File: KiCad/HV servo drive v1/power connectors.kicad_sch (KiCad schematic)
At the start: 12 parts, among them J10 DC BUS J2, J5 MOTOR, J7 DC BUS J1

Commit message: KiCad 8.0 update
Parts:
- renumbered C8 to C48, C9 to C49, C48 to C8, C49 to C9, J5 to J2, J7 to J4, J10 to J5

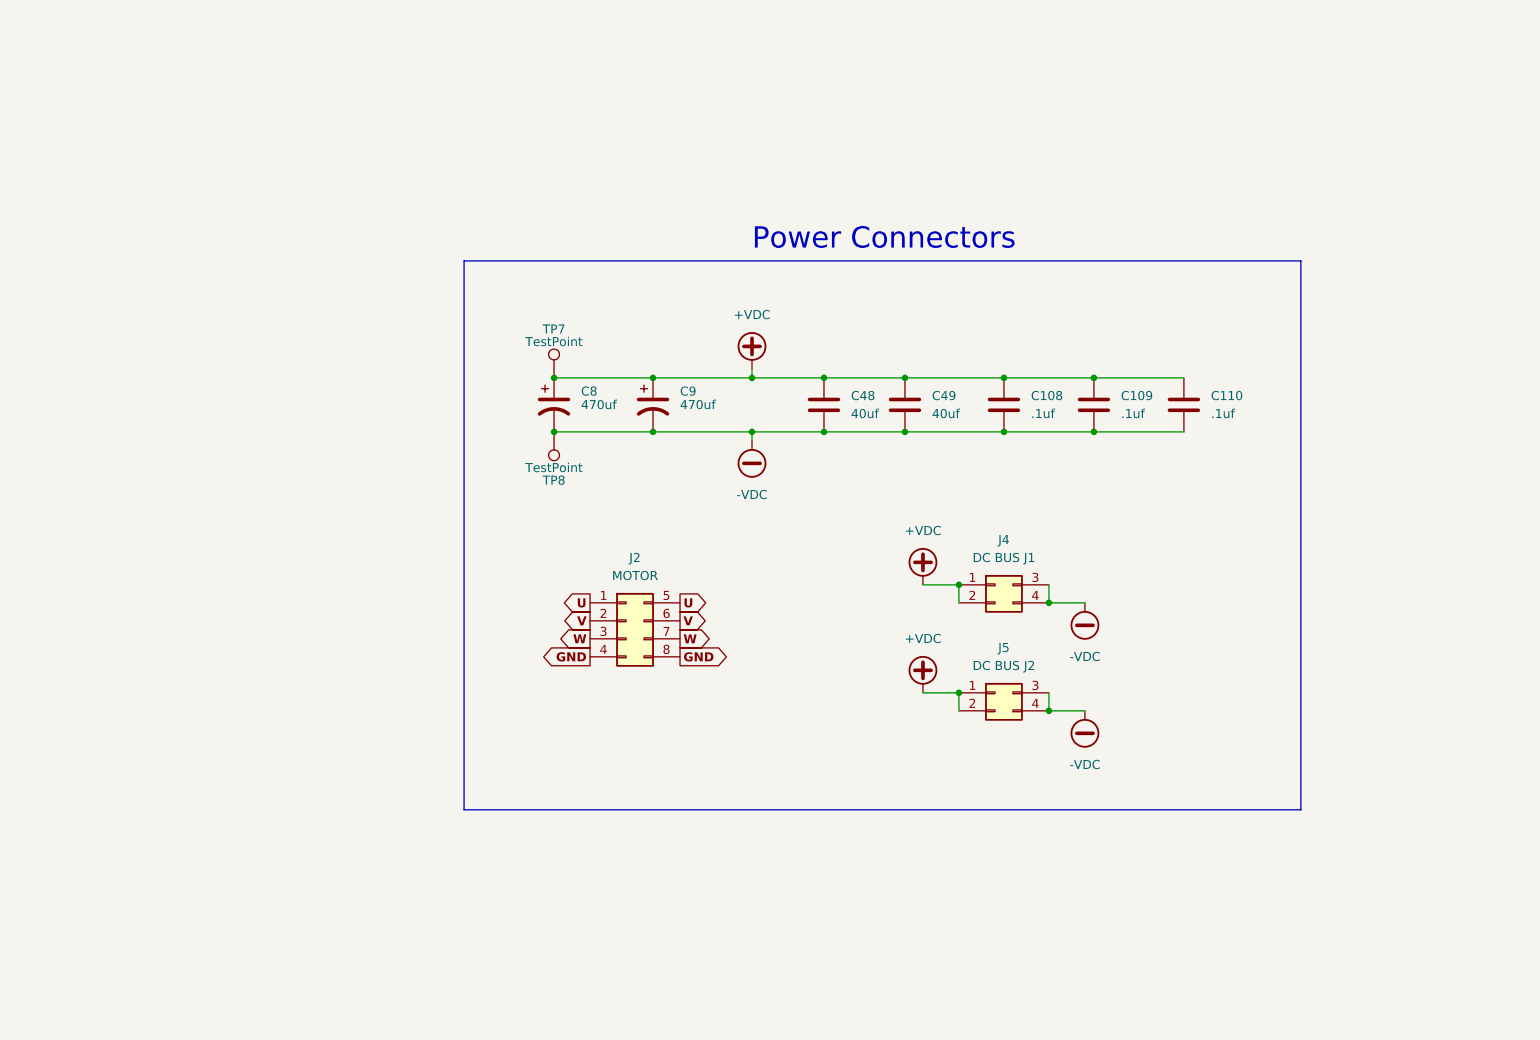
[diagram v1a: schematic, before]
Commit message: start rev 2 changes
fix component references, fix rj45 and dc-dc converter footprints, add RLC filters on all power connectors, add more mounting holes
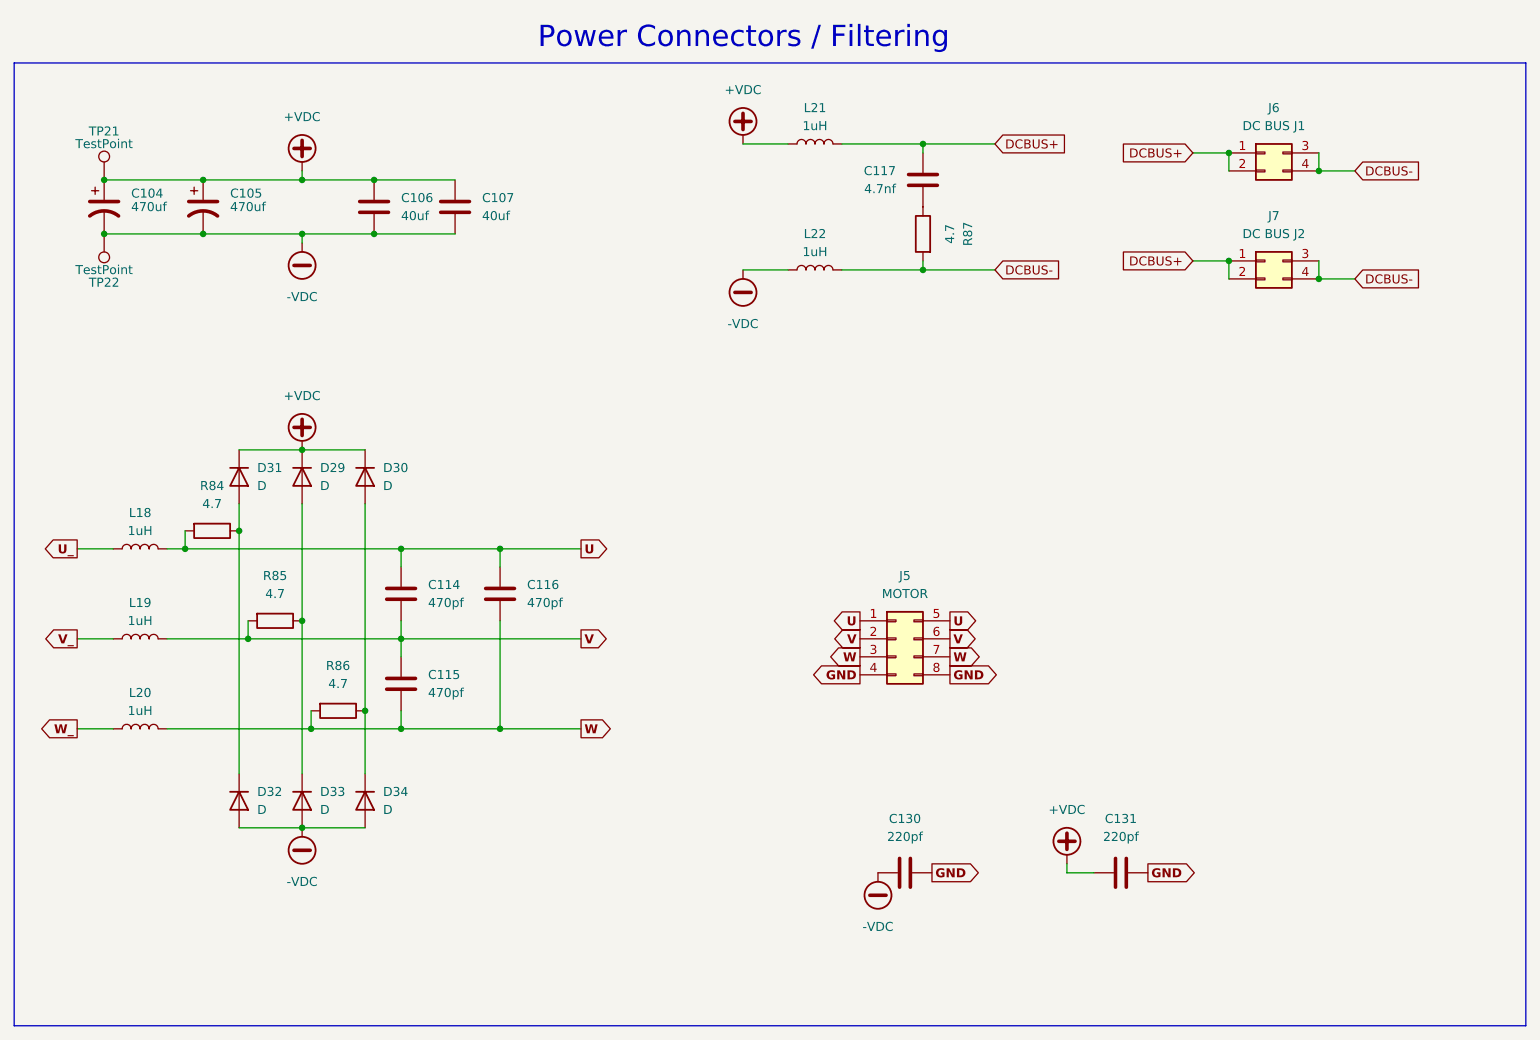
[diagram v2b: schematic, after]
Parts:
- removed C108, C109, C110: .1uf, Capacitor_SMD:C_2220_5650Metric, symbol Device:C
- added C114, C115, C116: 470pf, Capacitor_SMD:C_1206_3216Metric, symbol Device:C
- added C117: 4.7nf, Capacitor_SMD:C_1206_3216Metric, symbol Device:C
- added C130, C131: 220pf, Capacitor_THT:C_Disc_D7.5mm_W5.0mm_P10.00mm, symbol Device:C
- added D29, D30, D31, D32, D33, D34: D, Diode_SMD:D_SMC, symbol Device:D
- added L18, L19, L20: 1uH, Inductor_SMD:L_Vishay_IHLP-6767, symbol Device:L
- added L21, L22: 1uH, Inductor_SMD:L_Vishay_IHLP-5050, symbol Device:L
- added R84, R85, R86, R87: 4.7, footprints:R_1206_3216Metric_Wide, symbol Device:R
- renumbered C8 to C104, C9 to C105, C48 to C106, C49 to C107, J2 to J5, J4 to J6, J5 to J7, TP7 to TP21, TP8 to TP22
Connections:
- net +VDC: now also C131.2, D29.1 (K), D30.1 (K), D31.1 (K), L21.2; no longer J6.1 (Pin_1), J6.2 (Pin_2), J7.1 (Pin_1), J7.2 (Pin_2)
- net -VDC: now also C130.2, D32.2 (A), D33.2 (A), D34.2 (A), L22.2; no longer J6.3 (Pin_3), J6.4 (Pin_4), J7.3 (Pin_3), J7.4 (Pin_4)
- net GND: now also C130.1, C131.1
- net U: now also C114.1, C116.1, L18.2, R84.2
- net V: now also C114.2, C115.1, L19.2, R85.2
- net W: now also C115.2, C116.2, L20.2, R86.2
- new net: C117.2, R87.1
- new net: D30.2 (A), D34.1 (K), R86.1
- new net: D31.2 (A), D32.1 (K), R84.1
- new net: D29.2 (A), D33.1 (K), R85.1
- new net DCBUS+: C117.1, J6.1 (Pin_1), J6.2 (Pin_2), J7.1 (Pin_1), J7.2 (Pin_2), L21.1
- new net DCBUS-: J6.3 (Pin_3), J6.4 (Pin_4), J7.3 (Pin_3), J7.4 (Pin_4), L22.1, R87.2
- new net U_: L18.1
- new net V_: L19.1
- new net W_: L20.1
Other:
- note added: "Power Connectors / Filtering"
- note removed: "Power Connectors"
- moved on the sheet: C104, C105, C106, C107, J5, J6, J7, TP21, TP22

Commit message: update to rev 2.1
basically the same version as in the FOC youtube video, with some minor issues fixed
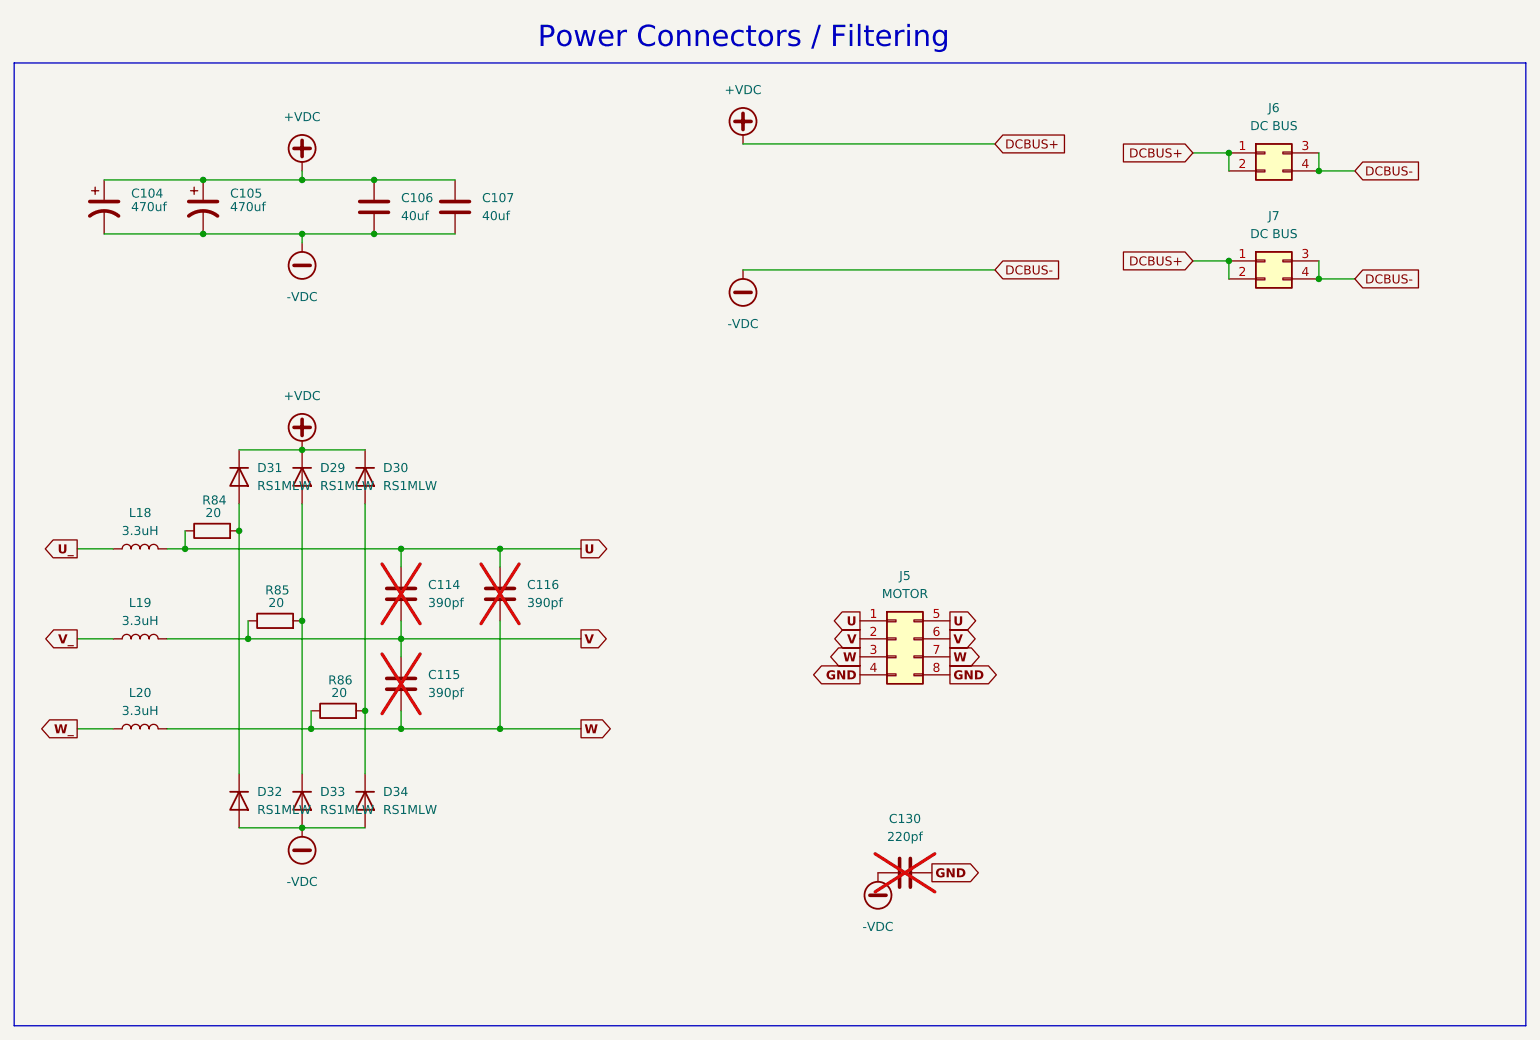
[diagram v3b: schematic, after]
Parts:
- removed C117: 4.7nf, Capacitor_SMD:C_1206_3216Metric, symbol Device:C
- removed C131: 220pf, Capacitor_THT:C_Disc_D7.5mm_W5.0mm_P10.00mm, symbol Device:C
- removed L21, L22: 1uH, Inductor_SMD:L_Vishay_IHLP-5050, symbol Device:L
- removed R87: 4.7, footprints:R_1206_3216Metric_Wide, symbol Device:R
- removed TP21, TP22: TestPoint, footprints:TestPoint_Pad_3.1x1.6mm, symbol Connector:TestPoint
- C104, C105: Generic Allowed? (none) -> yes; Manufacturer (none) -> Chemi-Con; Part number (none) -> ESMQ451VSN471MR45S
- C106, C107: Generic Allowed? (none) -> no; Manufacturer (none) -> KEMET; Part number (none) -> C4AQCBW5400A3LJ
- C114, C115, C116: value 470pf -> 390pf; footprint Capacitor_SMD:C_1206_3216Metric -> footprints:B326712L-SMD; Generic Allowed? (none) -> no; Manufacturer (none) -> TDK Corporation; Part number (none) -> CC45SL3AD391JYVNA; now not fitted
- C130: Generic Allowed? (none) -> yes; Manufacturer (none) -> Murata Electronics; Part number (none) -> DE1B3RA221KN4AP01F; now not fitted
- D29, D30, D31, D32, D33, D34: value D -> RS1MLW; footprint Diode_SMD:D_SMC -> footprints:D_SOD-123W; Generic Allowed? (none) -> yes; Manufacturer (none) -> Taiwan Semiconductor Corporation; Part number (none) -> RS1MLW
- J5: Generic Allowed? (none) -> yes; Manufacturer (none) -> Molex; Part number (none) -> 0768250008
- J6: value DC BUS J1 -> DC BUS; Generic Allowed? (none) -> yes; Manufacturer (none) -> Molex; Part number (none) -> 0768250004
- J7: value DC BUS J2 -> DC BUS; Generic Allowed? (none) -> yes; Manufacturer (none) -> Molex; Part number (none) -> 0768250004
- L18, L19, L20: value 1uH -> 3.3uH; Generic Allowed? (none) -> yes; Manufacturer (none) -> Vishay Dale; Part number (none) -> IHLP6767GZER3R3M01
- R84, R85, R86: value 4.7 -> 20; footprint footprints:R_1206_3216Metric_Wide -> Resistor_SMD:R_1210_3225Metric; Generic Allowed? (none) -> no; Manufacturer (none) -> Vishay Dale; Part number (none) -> CRCW121020R0JNEAHP
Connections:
- net DCBUS+ is gone; now on net +VDC: J6.1 (Pin_1), J6.2 (Pin_2), J7.1 (Pin_1), J7.2 (Pin_2)
- net DCBUS- is gone; now on net -VDC: J6.3 (Pin_3), J6.4 (Pin_4), J7.3 (Pin_3), J7.4 (Pin_4)
- net U: now also C114.2, R84.1; no longer C114.1, R84.2
- net V: now also C114.1, C115.2, R85.1; no longer C114.2, C115.1, R85.2
- net W: now also C115.1, R86.1; no longer C115.2, R86.2
- net at D30.2 (A), D34.1 (K): now also R86.2; no longer R86.1
- net at D31.2 (A), D32.1 (K): now also R84.2; no longer R84.1
- net at D29.2 (A), D33.1 (K): now also R85.2; no longer R85.1
